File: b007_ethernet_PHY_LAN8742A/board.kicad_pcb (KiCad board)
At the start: 4 copper layers, 21 x 29 mm, 34 parts, among them J1 011_GPIO_2x2, J6 006_RMII_2x10, J7 009_1000BASE-T_2x5, U4 LAN8742A, Y1 25MHz

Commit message: modernized connectors
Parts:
- removed J6: 006_RMII_2x10, on_edge:on_edge_2x10_device
- added J2: 006_RMII_2x10, on_edge:on_edge_2x10_device, F.Cu at (229.0, 59.5)
- FB1: value bead -> 600R
- FB2: value Ferrite_Bead_Small -> 600R
- J1: footprint on_edge:on_edge_2x02_host -> on_edge:on_edge_2x05_host
- moved R23 1.97 mm to (240.3, 64.0)
- moved C9 1.14 mm to (246.8, 65.5), turned to 0 degrees
- moved C10 1.12 mm to (248.7, 65.5), turned to 180 degrees
- moved R17 1.10 mm to (241.3, 64.0)
- moved R18 1.10 mm to (244.3, 64.0)
- moved R19 1.10 mm to (242.3, 64.0)
- moved R22 1.10 mm to (243.3, 64.0)
- moved R15 0.80 mm to (238.2, 64.6)
- moved R24 0.80 mm to (239.2, 64.6)
- moved R16 0.80 mm to (237.5, 63.1)
- moved Y1 0.55 mm to (247.6, 68.2)
- moved C12 0.37 mm to (241.7, 66.1)
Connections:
- C10 pad 2: /phy/GND -> GND
- C11 pad 2: /phy/GND -> GND
- C12 pad 2: /phy/GND -> GND
- C13 pad 2: /phy/GND -> GND
- C14 pad 2: /phy/GND -> GND
- C15 pad 1: /phy/ETH_VDD -> /phy/3v3_in
- C15 pad 2: /phy/GND -> GND
- C16 pad 1: /phy/ETH_VDD -> /phy/3v3_in
- C16 pad 2: /phy/GND -> GND
- C17 pad 1: /phy/ETH_VDD -> /phy/3v3_in
- C17 pad 2: /phy/GND -> GND
- C18 pad 1: /phy/ETH_VDD -> /phy/3v3_in
- C18 pad 2: /phy/GND -> GND
- C19 pad 1: /phy/ETH_VDD -> /phy/3v3_in
- C19 pad 2: /phy/GND -> GND
- C9 pad 2: /phy/GND -> GND
- FB2 pad 2: /phy/ETH_VDD -> /phy/3v3_in
- J1 pad 1: /phy/GND -> GND
- J1 pad 2: /phy/3v3_in -> /phy/LED1
- J1 pad 3: /phy/LED1 -> /phy/LED2
- J1 pad 4: /phy/LED2 -> (no net)
- J7 pad 1: /phy/GND -> GND
- J7 pad 3: /phy/GND -> Net-(J7-Pad3)
- J7 pad 4: (no net) -> Net-(J7-Pad4)
- J7 pad 6: (no net) -> GND
- J7 pad 7: Net-(J7-Pad7) -> (no net)
- J7 pad 9: Net-(J7-Pad9) -> (no net)
- R19 pad 1: /phy/GND -> GND
- R22 pad 1: /phy/GND -> GND
- R23 pad 2: /phy/GND -> GND
- R26 pad 1: /phy/ETH_VDD -> /phy/3v3_in
- R26 pad 2: Net-(J7-Pad9) -> Net-(J7-Pad5)
- R30 pad 2: /phy/GND -> GND
- R31 pad 1: /phy/ETH_VDD -> /phy/3v3_in
- R31 pad 2: Net-(J7-Pad5) -> Net-(J7-Pad4)
- R33 pad 1: /phy/ETH_VDD -> /phy/3v3_in
- R33 pad 2: Net-(J7-Pad2) -> Net-(J7-Pad3)
- R34 pad 2: /phy/GND -> GND
- R35 pad 1: /phy/ETH_VDD -> /phy/3v3_in
- R35 pad 2: Net-(J7-Pad7) -> Net-(J7-Pad2)
- U4 pad 1: /phy/ETH_VDD -> /phy/3v3_in
- U4 pad 19: /phy/ETH_VDD -> /phy/3v3_in
- U4 pad 20: Net-(J7-Pad2) -> Net-(J7-Pad3)
- U4 pad 21: Net-(J7-Pad7) -> Net-(J7-Pad2)
- U4 pad 22: Net-(J7-Pad9) -> Net-(J7-Pad5)
- U4 pad 23: Net-(J7-Pad5) -> Net-(J7-Pad4)
- U4 pad 25: /phy/GND -> GND
- Y1 pad 2: /phy/GND -> GND
- Y1 pad 4: /phy/GND -> GND
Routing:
- net /phy/GND: track 118.8 -> 0.00 mm, vias 17 -> 0
- net GND: track 0.00 -> 117.9 mm, vias 0 -> 15
- net /phy/3v3_in: track 24.6 -> 57.3 mm, vias 2 -> 4
- net /phy/ETH_VDD: track 31.3 -> 0.00 mm, vias 2 -> 0
- net Net-(J7-Pad7): track 12.3 -> 0.00 mm, vias 2 -> 0
- net Net-(J7-Pad4): track 0.00 -> 10.8 mm
- net Net-(J7-Pad9): track 10.7 -> 0.00 mm
- net Net-(J7-Pad3): track 0.00 -> 8.81 mm, vias 0 -> 2
- net /phy/MDC: track 9.47 -> 16.2 mm
- net /phy/3v3: track 31.1 -> 37.2 mm
- net /phy/MDIO: track 11.3 -> 17.3 mm, vias 2 -> 1
- net /phy/TXEN: track 20.5 -> 15.6 mm, vias 0 -> 2
- net /phy/LED1: track 19.6 -> 15.6 mm
- net /phy/CRS_DV: track 13.0 -> 16.8 mm, vias 1 -> 2
- net /phy/LED2: track 22.1 -> 18.4 mm
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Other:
- board text added: "osf.b007.v0.2"
- board text removed: "osf.b007.v0.1"

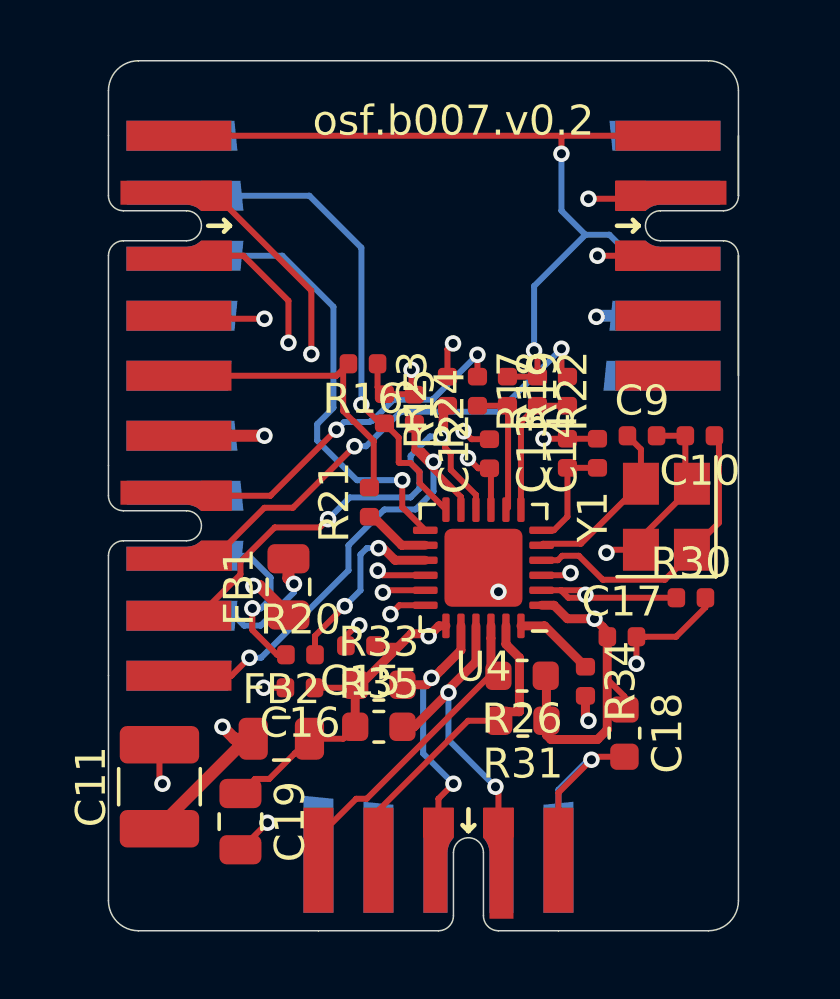
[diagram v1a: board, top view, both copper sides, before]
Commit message: changed b007 to new plugs and 0603 as smalles component size
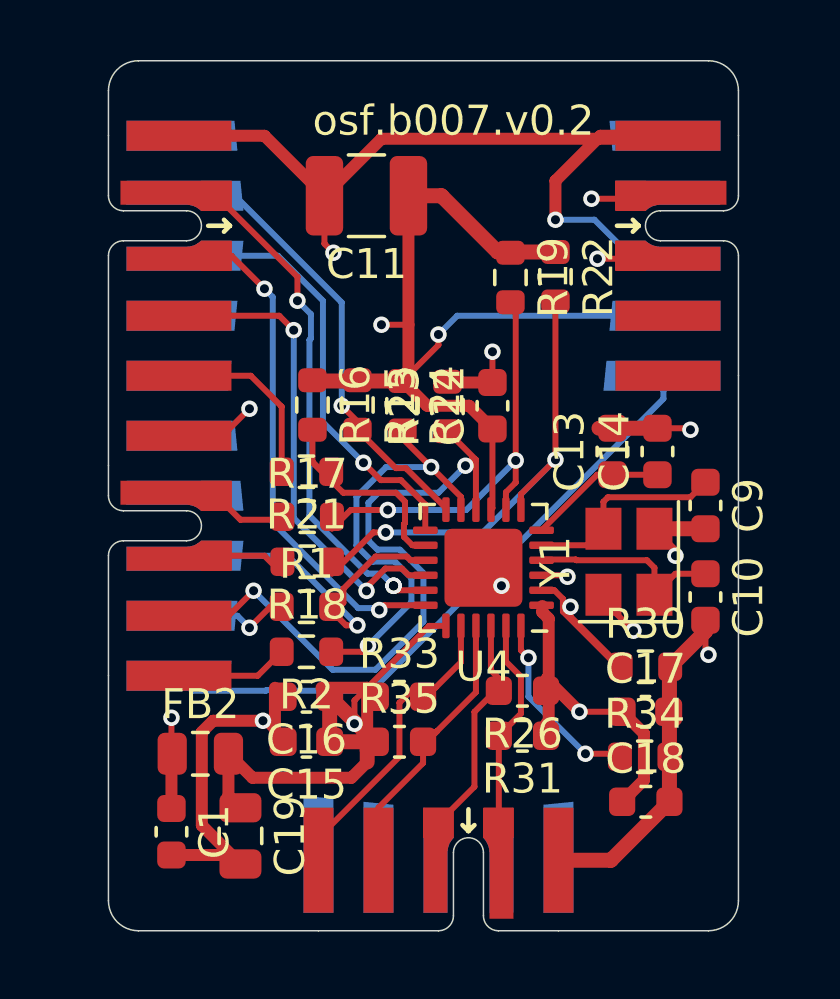
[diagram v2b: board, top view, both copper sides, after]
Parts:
- removed FB1: 600R, Inductor_SMD:L_0805_2012Metric
- removed J7: 009_1000BASE-T_2x5, on_edge:on_edge_2x05_host
- removed R20: 33R, Resistor_SMD:R_0402_1005Metric
- added C1: 100nF, Capacitor_SMD:C_0603_1608Metric, F.Cu at (231.1, 78.7)
- added J3: 011_GPIO_2x2, on_edge:on_edge_2x05_host, F.Cu at (250.0, 59.5)
- added R1: 10k, Resistor_SMD:R_0603_1608Metric, F.Cu at (235.6, 71.2)
- added R2: 33R, Resistor_SMD:R_0603_1608Metric, F.Cu at (235.6, 72.7)
- C10, C9: value TBD -> 13pF; footprint Capacitor_SMD:C_0402_1005Metric -> Capacitor_SMD:C_0603_1608Metric
- C12, C13, C14, C15, C16, C17: footprint Capacitor_SMD:C_0402_1005Metric -> Capacitor_SMD:C_0603_1608Metric
- J1: value 011_GPIO_2x2 -> 009_1000BASE-T_2x5
- R15, R16, R17, R18, R19, R21, R22, R24, R30, R34: footprint Resistor_SMD:R_0402_1005Metric -> Resistor_SMD:R_0603_1608Metric
- R23: value 33R -> 10k; footprint Resistor_SMD:R_0402_1005Metric -> Resistor_SMD:R_0603_1608Metric
- moved J1 24.6 mm to (240.0, 82.0), turned to 180 degrees
- moved C11 20.9 mm to (237.6, 57.5), turned to 180 degrees
- moved R18 10.4 mm to (235.6, 69.7), turned to 180 degrees
- moved R17 7.05 mm to (235.6, 68.2), turned to 0 degrees
- moved C10 5.38 mm to (248.9, 70.9), turned to 270 degrees
- moved R22 3.86 mm to (243.9, 60.2)
- moved R19 3.79 mm to (242.4, 60.2)
- moved C15 3.67 mm to (235.6, 75.7)
- moved R34 3.20 mm to (246.9, 76.2), turned to 0 degrees
- moved C9 3.14 mm to (248.9, 67.8), turned to 270 degrees
- moved R30 2.75 mm to (246.9, 73.2)
- moved FB2 2.75 mm to (232.1, 76.1)
- moved C17 2.62 mm to (246.9, 74.7)
- moved C18 2.40 mm to (246.9, 77.7), turned to 0 degrees
- moved R21 2.33 mm to (235.6, 66.7), turned to 180 degrees
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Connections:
- C11 pad 1: /phy/3v3 -> /phy/3v3_in
- C12 pad 1: /phy/3v3 -> /phy/3v3_in
- C15 pad 1: /phy/3v3_in -> /phy/ETH_VDD
- C16 pad 1: /phy/3v3_in -> /phy/ETH_VDD
- C17 pad 1: /phy/3v3_in -> /phy/ETH_VDD
- C18 pad 1: /phy/3v3_in -> /phy/ETH_VDD
- C19 pad 1: /phy/3v3_in -> /phy/ETH_VDD
- FB2 pad 1: /phy/3v3 -> /phy/3v3_in
- FB2 pad 2: /phy/3v3_in -> /phy/ETH_VDD
- J1 pad 2: /phy/LED1 -> /phy/TD1+
- J1 pad 3: /phy/LED2 -> /phy/TD1-
- J1 pad 4: (no net) -> /phy/TD2+
- J1 pad 5: (no net) -> /phy/TD2-
- J1 pad 6: (no net) -> GND
- J1 pad 8: GND -> (no net)
- J1 pad 9: /phy/3v3_in -> (no net)
- J2 pad 20: (no net) -> Net-(J2-Pad20)
- R15 pad 1: /phy/3v3 -> /phy/3v3_in
- R16 pad 1: /phy/3v3 -> /phy/3v3_in
- R16 pad 2: /phy/INT_REFCLK -> Net-(R16-Pad2)
- R19 pad 1: GND -> /phy/3v3_in
- R21 pad 1: Net-(R21-Pad1) -> Net-(R16-Pad2)
- R22 pad 1: GND -> /phy/3v3_in
- R24 pad 1: /phy/3v3 -> /phy/3v3_in
- R24 pad 2: /phy/CRS_DV -> Net-(R2-Pad1)
- R26 pad 1: /phy/3v3_in -> /phy/ETH_VDD
- R26 pad 2: Net-(J7-Pad5) -> /phy/TD1-
- R31 pad 1: /phy/3v3_in -> /phy/ETH_VDD
- R31 pad 2: Net-(J7-Pad4) -> /phy/TD1+
- R33 pad 1: /phy/3v3_in -> /phy/ETH_VDD
- R33 pad 2: Net-(J7-Pad3) -> /phy/TD2-
- R35 pad 1: /phy/3v3_in -> /phy/ETH_VDD
- R35 pad 2: Net-(J7-Pad2) -> /phy/TD2+
- U4 pad 1: /phy/3v3_in -> /phy/ETH_VDD
- U4 pad 11: /phy/CRS_DV -> Net-(R2-Pad1)
- U4 pad 14: Net-(R21-Pad1) -> Net-(R16-Pad2)
- U4 pad 15: Net-(R20-Pad2) -> /phy/~RST
- U4 pad 19: /phy/3v3_in -> /phy/ETH_VDD
- U4 pad 20: Net-(J7-Pad3) -> /phy/TD2-
- U4 pad 21: Net-(J7-Pad2) -> /phy/TD2+
- U4 pad 22: Net-(J7-Pad5) -> /phy/TD1-
- U4 pad 23: Net-(J7-Pad4) -> /phy/TD1+
- U4 pad 9: /phy/3v3 -> /phy/3v3_in
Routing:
- net /phy/ETH_VDD: track 0.00 -> 40.3 mm, vias 0 -> 2
- net /phy/3v3: track 37.2 -> 0.00 mm, vias 4 -> 0
- net Net-(J2-Pad20): track 0.00 -> 21.2 mm
- net Net-(R2-Pad1): track 0.00 -> 14.4 mm, vias 0 -> 2
- net /phy/CRS_DV: track 16.8 -> 3.76 mm, vias 2 -> 0
- net /phy/RXD1: track 15.4 -> 2.45 mm, vias 2 -> 0
- net Net-(R18-Pad1): track 4.69 -> 16.4 mm, vias 0 -> 2
- net Net-(J7-Pad5): track 10.8 -> 0.00 mm
- net Net-(J7-Pad4): track 10.8 -> 0.00 mm
- net /phy/TD2-: track 0.00 -> 10.2 mm
- net Net-(R17-Pad2): track 4.50 -> 14.2 mm, vias 0 -> 2
- net /phy/TD2+: track 0.00 -> 9.64 mm
- net Net-(J7-Pad2): track 9.64 -> 0.00 mm, vias 2 -> 0
- net /phy/RXD0: track 11.4 -> 2.53 mm, vias 2 -> 0
- net Net-(J7-Pad3): track 8.81 -> 0.00 mm, vias 2 -> 0
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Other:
- outline, holes or cut-outs redrawn

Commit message: updated ethernet connector
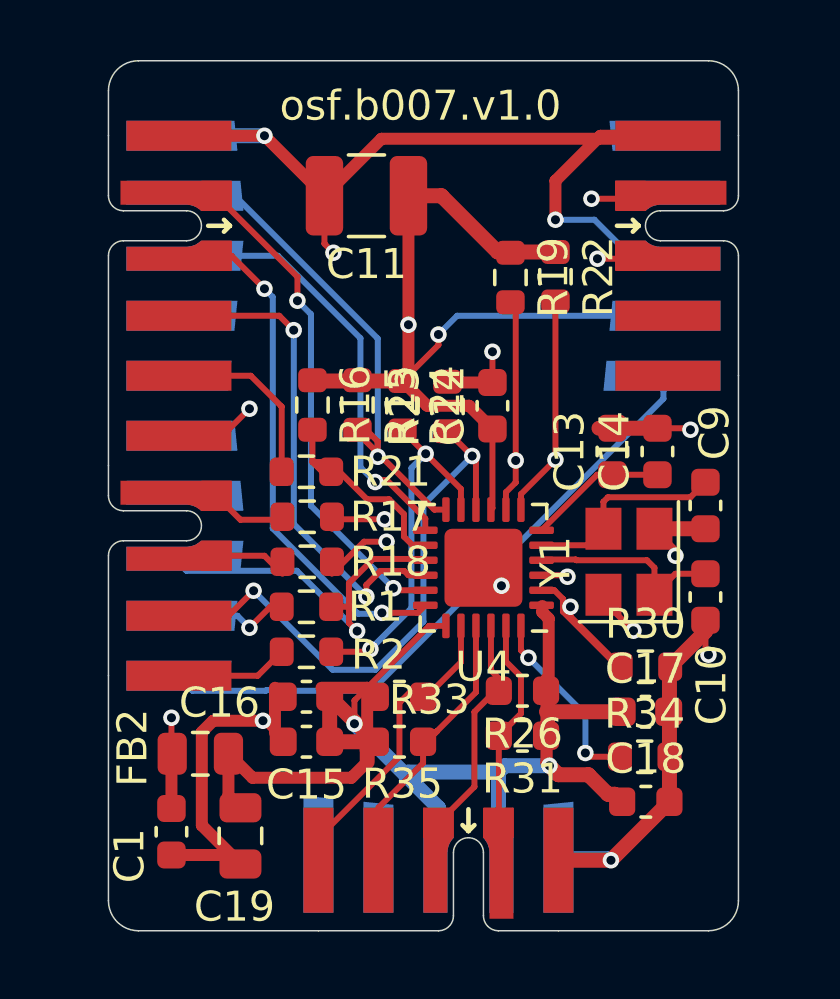
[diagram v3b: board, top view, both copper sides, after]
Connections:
- C15 pad 1: /phy/ETH_VDD -> /phy/CT
- C16 pad 1: /phy/ETH_VDD -> /phy/CT
- C17 pad 1: /phy/ETH_VDD -> /phy/CT
- C18 pad 1: /phy/ETH_VDD -> /phy/CT
- C19 pad 1: /phy/ETH_VDD -> /phy/CT
- FB2 pad 2: /phy/ETH_VDD -> /phy/CT
- J1 pad 7: (no net) -> /phy/CT
- J1 pad 8: (no net) -> /phy/CT
- R26 pad 1: /phy/ETH_VDD -> /phy/CT
- R31 pad 1: /phy/ETH_VDD -> /phy/CT
- R33 pad 1: /phy/ETH_VDD -> /phy/CT
- R35 pad 1: /phy/ETH_VDD -> /phy/CT
- U4 pad 1: /phy/ETH_VDD -> /phy/CT
- U4 pad 19: /phy/ETH_VDD -> /phy/CT
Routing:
- net /phy/CT: track 0.00 -> 49.3 mm, vias 0 -> 2
- net /phy/ETH_VDD: track 40.3 -> 0.00 mm, vias 2 -> 0
- net GND: track 118.0 -> 122.6 mm, vias 10 -> 12
- net /phy/RX_ER: track 22.6 -> 19.6 mm
- net /phy/MDIO: track 15.8 -> 18.1 mm
- net Net-(R2-Pad1): track 14.4 -> 12.1 mm
- net /phy/TXD0: track 16.9 -> 16.6 mm, vias 3 -> 2
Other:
- board text added: "osf.b007.v1.0"
- board text removed: "osf.b007.v0.2"
